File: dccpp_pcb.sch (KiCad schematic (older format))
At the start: 60 parts, among them J1 USB_B_Micro, J10 OSTTC022162, J11 OSTTC022162, J12 OSTTC022162, J2 AVR-ISP-6, J3 OSTTC022162, J4 OSTTC022162, J5 OSTTC022162, J6 OSTTC022162, J7 OSTTC022162, J8 OSTTC022162, J9 OSTTC022162, U1 ATmega32U4-AU, U2 74HC04, U3 IFX007T, U4 IFX007T, U5 IFX007T, U6 IFX007T, Y1 16MHz

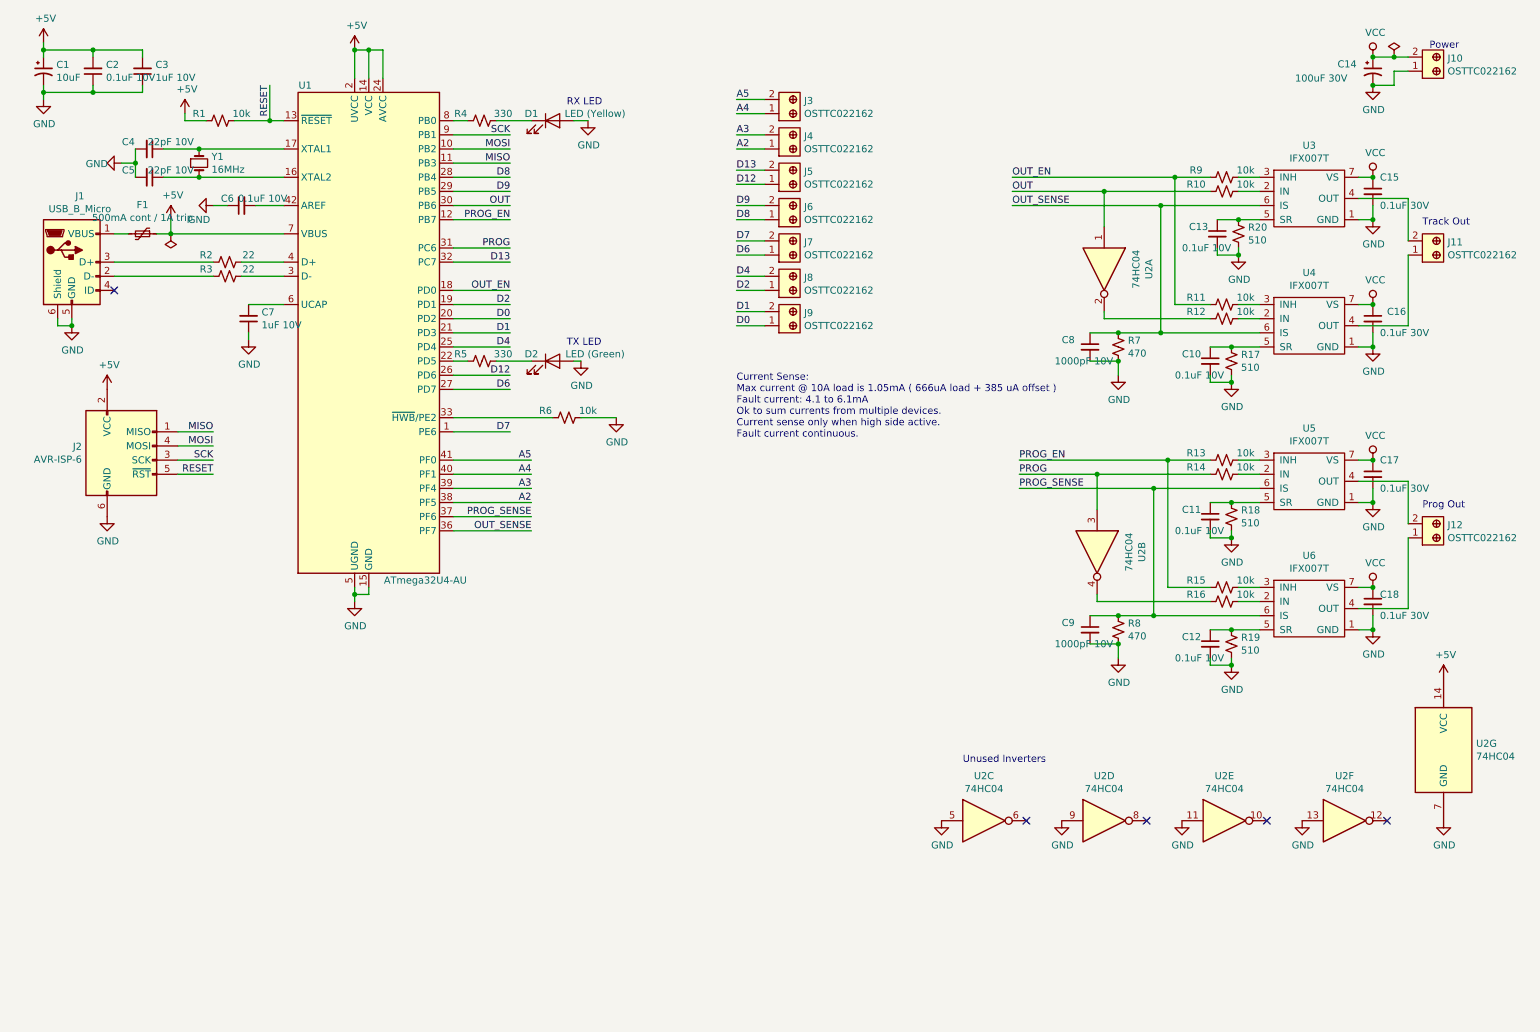
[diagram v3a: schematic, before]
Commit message: Setup design rules
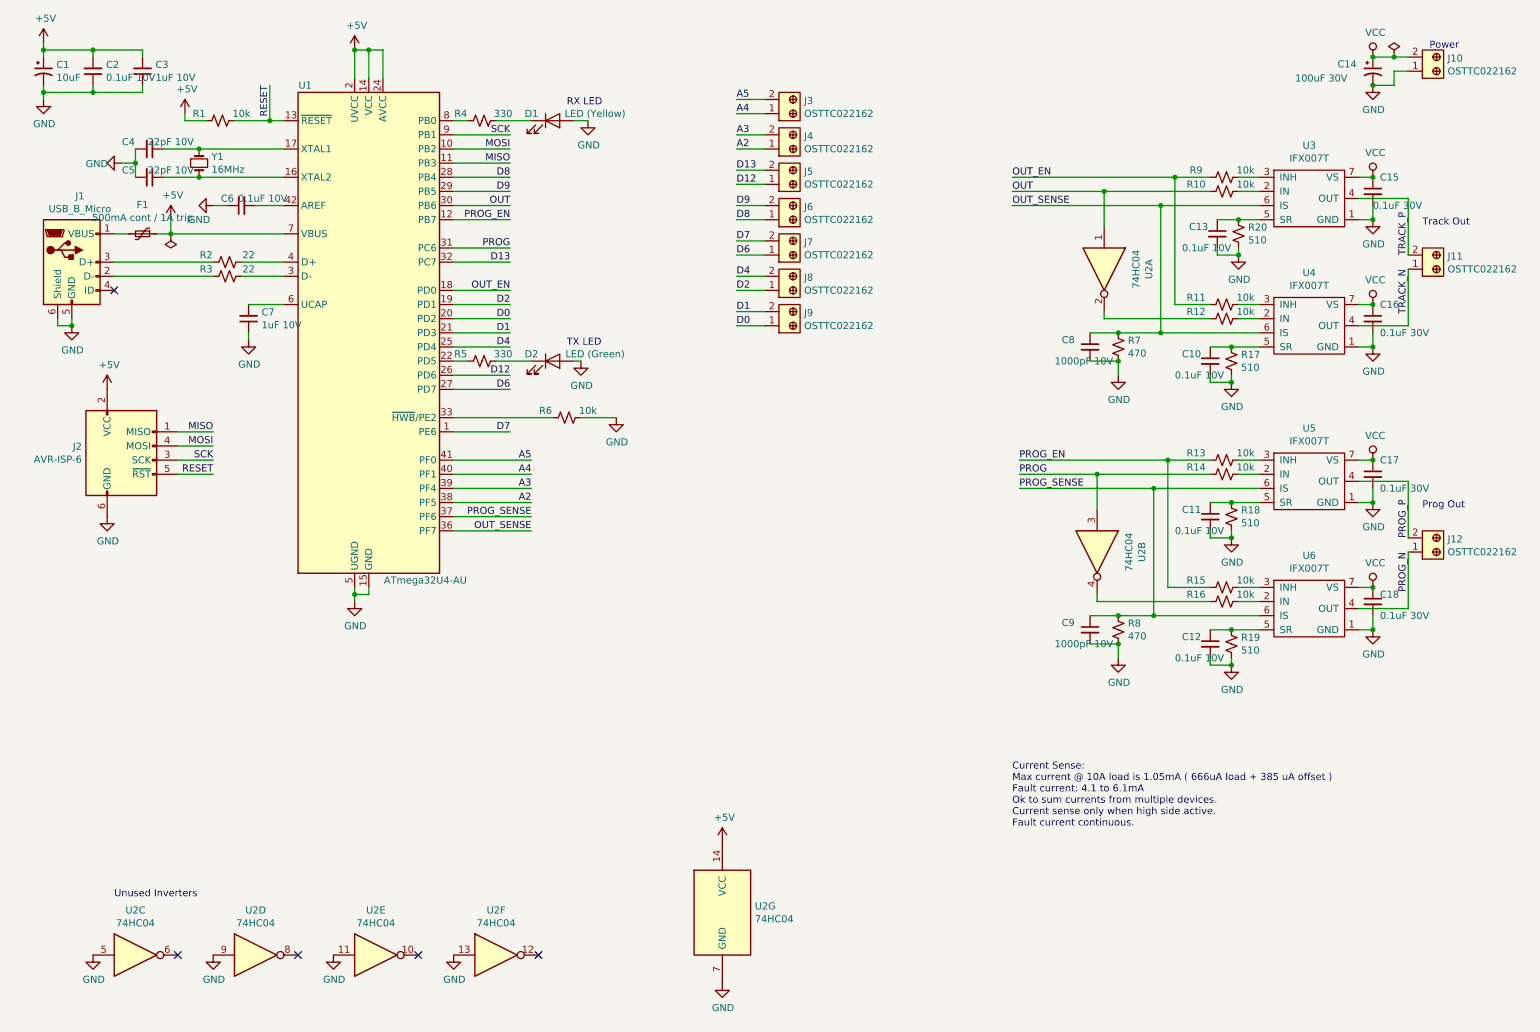
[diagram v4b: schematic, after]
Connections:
- net TRACK_N: now reaches J11.1, U4.4 (OUT), U4.8 (OUT)
- net TRACK_P: now reaches J11.2, U3.4 (OUT), U3.8 (OUT)
- net PROG_P: now reaches J12.2, U5.4 (OUT), U5.8 (OUT)
- net PROG_N: now reaches J12.1, U6.4 (OUT), U6.8 (OUT)
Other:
- moved on the sheet: J11, J12, U2C, U2D, U2E, U2F, U2G

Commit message: Start work on signal layout.
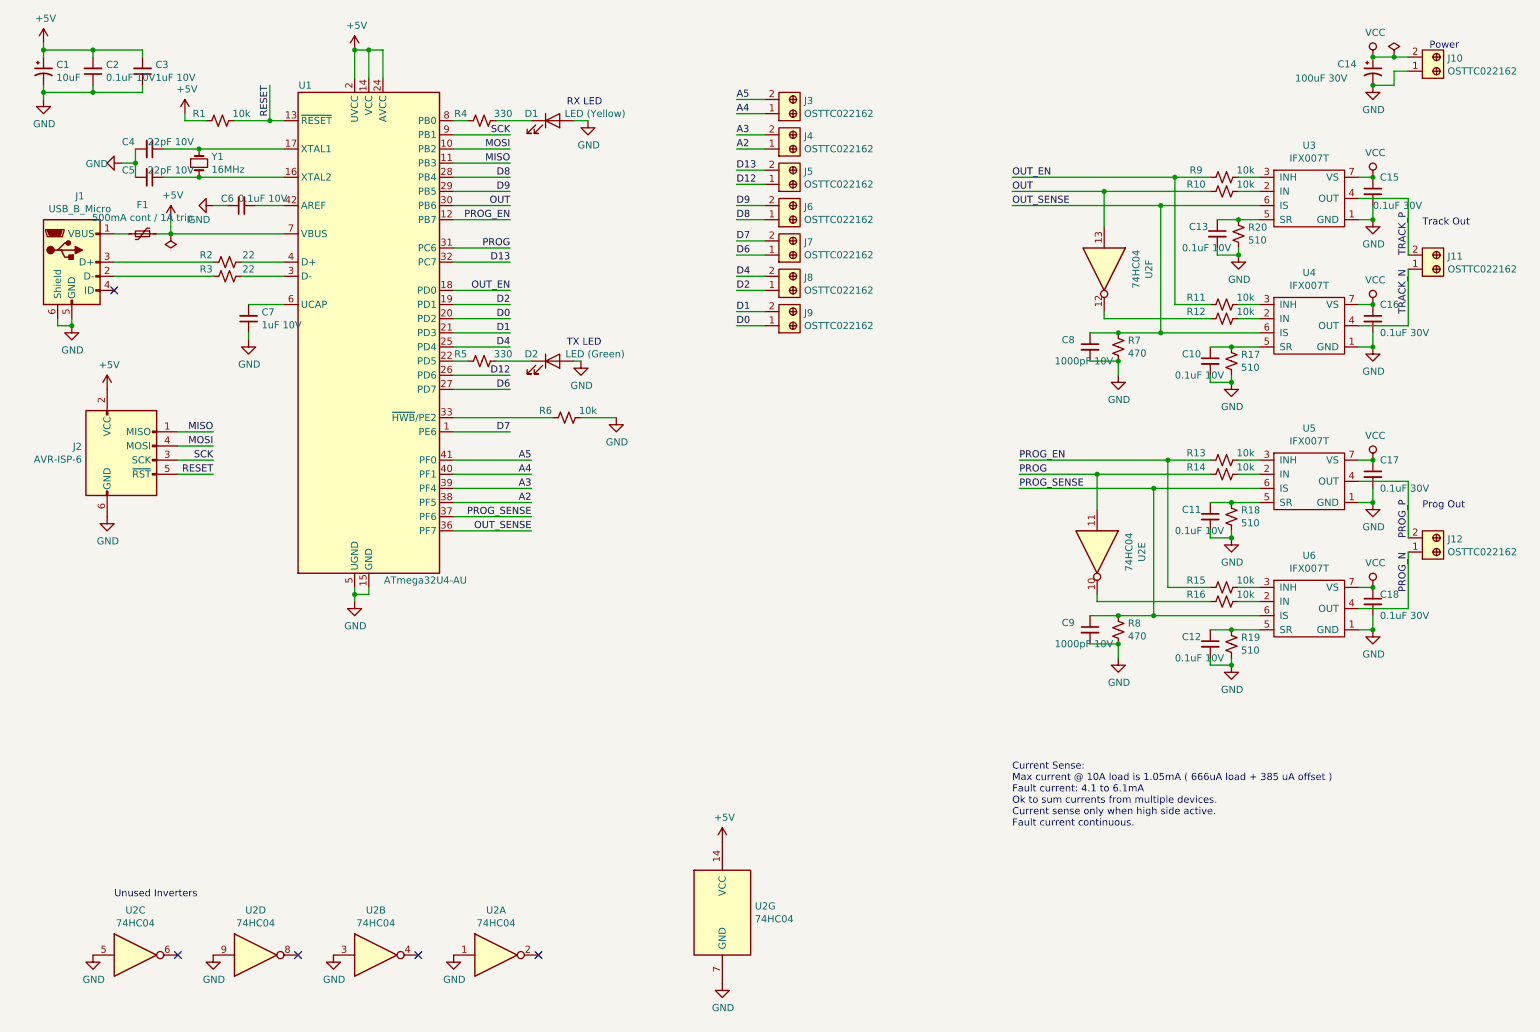
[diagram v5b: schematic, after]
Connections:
- net GND: now also U2.1, U2.3; no longer U2.11, U2.13
- net OUT: now also U2.13; no longer U2.1
- net PROG: now also U2.11; no longer U2.3
- net at U2.2: no longer R12.2
- net at U2.4: no longer R16.2
- net at U2.10: now also R16.2
- net at U2.12: now also R12.2
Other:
- moved on the sheet: U2A, U2B, U2E, U2F
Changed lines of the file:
@@
 EESchema Schematic File Version 4
-LIBS:dccpp_pcb-cache
 EELAYER 29 0
 EELAYER END
@@
 L 74xx:74HC04 U2
 U 1 1 5CF642FD
-P 8200 2350
-F 0 "U2" H 8200 2667 50  0000 C CNN
-F 1 "74HC04" H 8200 2576 50  0000 C CNN
-F 2 "Package_SO:SOIC-14_3.9x8.7mm_P1.27mm" H 8200 2350 50  0001 C CNN
-F 3 "https://assets.nexperia.com/documents/data-sheet/74HC_HCT04.pdf" H 8200 2350 50  0001 C CNN
-F 4 "MC74HC04ADGOS-ND" H 8200 2350 50  0001 C CNN "Digi-Key_PN"
-F 5 "MC74HC04ADG" H 8200 2350 50  0001 C CNN "MPN"
-	1    8200 2350
-	0    1    1    0
+P 3900 7200
+F 0 "U2" H 3900 7517 50  0000 C CNN
+F 1 "74HC04" H 3900 7426 50  0000 C CNN
+F 2 "Package_SO:SOIC-14_3.9x8.7mm_P1.27mm" H 3900 7200 50  0001 C CNN
+F 3 "https://assets.nexperia.com/documents/data-sheet/74HC_HCT04.pdf" H 3900 7200 50  0001 C CNN
+F 4 "MC74HC04ADGOS-ND" H 3900 7200 50  0001 C CNN "Digi-Key_PN"
+F 5 "MC74HC04ADG" H 3900 7200 50  0001 C CNN "MPN"
+	1    3900 7200
+	1    0    0    -1
 $EndComp
 $Comp
 L 74xx:74HC04 U2
 U 2 1 5CF6599A
-P 8150 4350
-F 0 "U2" H 8150 4667 50  0000 C CNN
-F 1 "74HC04" H 8150 4576 50  0000 C CNN
-F 2 "Package_SO:SOIC-14_3.9x8.7mm_P1.27mm" H 8150 4350 50  0001 C CNN
-F 3 "https://assets.nexperia.com/documents/data-sheet/74HC_HCT04.pdf" H 8150 4350 50  0001 C CNN
-F 4 "MC74HC04ADGOS-ND" H 8150 4350 50  0001 C CNN "Digi-Key_PN"
-F 5 "MC74HC04ADG" H 8150 4350 50  0001 C CNN "MPN"
-	2    8150 4350
-	0    1    1    0
+P 3050 7200
+F 0 "U2" H 3050 7517 50  0000 C CNN
+F 1 "74HC04" H 3050 7426 50  0000 C CNN
+F 2 "Package_SO:SOIC-14_3.9x8.7mm_P1.27mm" H 3050 7200 50  0001 C CNN
+F 3 "https://assets.nexperia.com/documents/data-sheet/74HC_HCT04.pdf" H 3050 7200 50  0001 C CNN
+F 4 "MC74HC04ADGOS-ND" H 3050 7200 50  0001 C CNN "Digi-Key_PN"
+F 5 "MC74HC04ADG" H 3050 7200 50  0001 C CNN "MPN"
+	2    3050 7200
+	1    0    0    -1
 $EndComp
 $Comp
@@
 L 74xx:74HC04 U2
 U 5 1 5CF770C1
-P 3050 7200
-F 0 "U2" H 3050 7517 50  0000 C CNN
-F 1 "74HC04" H 3050 7426 50  0000 C CNN
-F 2 "Package_SO:SOIC-14_3.9x8.7mm_P1.27mm" H 3050 7200 50  0001 C CNN
-F 3 "https://assets.nexperia.com/documents/data-sheet/74HC_HCT04.pdf" H 3050 7200 50  0001 C CNN
-F 4 "MC74HC04ADGOS-ND" H 3050 7200 50  0001 C CNN "Digi-Key_PN"
-F 5 "MC74HC04ADG" H 3050 7200 50  0001 C CNN "MPN"
-	5    3050 7200
-	1    0    0    -1
+P 8150 4350
+F 0 "U2" H 8150 4667 50  0000 C CNN
+F 1 "74HC04" H 8150 4576 50  0000 C CNN
+F 2 "Package_SO:SOIC-14_3.9x8.7mm_P1.27mm" H 8150 4350 50  0001 C CNN
+F 3 "https://assets.nexperia.com/documents/data-sheet/74HC_HCT04.pdf" H 8150 4350 50  0001 C CNN
+F 4 "MC74HC04ADGOS-ND" H 8150 4350 50  0001 C CNN "Digi-Key_PN"
+F 5 "MC74HC04ADG" H 8150 4350 50  0001 C CNN "MPN"
+	5    8150 4350
+	0    1    1    0
 $EndComp
 $Comp
 L 74xx:74HC04 U2
 U 6 1 5CF77E52
-P 3900 7200
-F 0 "U2" H 3900 7517 50  0000 C CNN
-F 1 "74HC04" H 3900 7426 50  0000 C CNN
-F 2 "Package_SO:SOIC-14_3.9x8.7mm_P1.27mm" H 3900 7200 50  0001 C CNN
-F 3 "https://assets.nexperia.com/documents/data-sheet/74HC_HCT04.pdf" H 3900 7200 50  0001 C CNN
-F 4 "MC74HC04ADGOS-ND" H 3900 7200 50  0001 C CNN "Digi-Key_PN"
-F 5 "MC74HC04ADG" H 3900 7200 50  0001 C CNN "MPN"
-	6    3900 7200
-	1    0    0    -1
-$EndComp
-$Comp
+P 8200 2350
+F 0 "U2" H 8200 2667 50  0000 C CNN
+F 1 "74HC04" H 8200 2576 50  0000 C CNN
+F 2 "Package_SO:SOIC-14_3.9x8.7mm_P1.27mm" H 8200 2350 50  0001 C CNN
+F 3 "https://assets.nexperia.com/documents/data-sheet/74HC_HCT04.pdf" H 8200 2350 50  0001 C CNN
+F 4 "MC74HC04ADGOS-ND" H 8200 2350 50  0001 C CNN "Digi-Key_PN"
+F 5 "MC74HC04ADG" H 8200 2350 50  0001 C CNN "MPN"
+	6    8200 2350
+	0    1    1    0
+$EndComp
+$Comp

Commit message: More routing
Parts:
- added C19, C20, C21, C22, C23, C24: 0.1uF 10V, Capacitor_SMD:C_0603_1608Metric_Pad1.05x0.95mm_HandSolder, symbol Device:C_Small
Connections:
- net +5V: now also C19.2, C20.2, C21.2, C22.2, C23.2, C24.2
- net GND: now also C19.1, C20.1, C21.1, C22.1, C23.1, C24.1
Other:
- note added: "Place 0.1uF decoupling caps near Vcc on U1 and U2"
- moved on the sheet: C1, C2, C3, C4, C5, C6, C7, D1, D2, F1, J1, J2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

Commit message: Fix crystal
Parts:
- Y1: symbol Device:Crystal_Small -> Device:Crystal_GND24_Small
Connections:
- wire segments 208 -> 210
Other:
- moved on the sheet: C7
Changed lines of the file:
@@
-$EndComp
-$Comp
-L Device:Crystal_Small Y1
-U 1 1 5CD9CF37
-P 1850 2100
-F 0 "Y1" V 1804 2188 50  0000 L CNN
-F 1 "16MHz" V 1895 2188 50  0000 L CNN
-F 2 "Crystal:Crystal_SMD_SeikoEpson_TSX3225-4Pin_3.2x2.5mm_HandSoldering" H 1850 2100 50  0001 C CNN
-F 3 "~" H 1850 2100 50  0001 C CNN
-F 4 "SER4069CT-ND" H 1850 2100 50  0001 C CNN "Digi-Key_PN"
-F 5 "TSX-3225 16.0000MF09Z-AC0" H 1850 2100 50  0001 C CNN "MPN"
-	1    1850 2100
-	0    1    1    0
 $EndComp
 $Comp
@@
 P 1500 2200
 F 0 "C5" V 1450 2050 50  0000 C CNN
-F 1 "22pF 10V" V 1450 2350 50  0000 C CNN
+F 1 "22pF 10V" V 1550 2450 50  0000 C CNN
 F 2 "Capacitor_SMD:C_0603_1608Metric_Pad1.05x0.95mm_HandSolder" H 1500 2200 50  0001 C CNN
 F 3 "~" H 1500 2200 50  0001 C CNN
@@
 P 1500 2000
 F 0 "C4" V 1450 1850 50  0000 C CNN
-F 1 "22pF 10V" V 1450 2150 50  0000 C CNN
+F 1 "22pF 10V" V 1450 2250 50  0000 C CNN
 F 2 "Capacitor_SMD:C_0603_1608Metric_Pad1.05x0.95mm_HandSolder" H 1500 2000 50  0001 C CNN
 F 3 "~" H 1500 2000 50  0001 C CNN
@@
 L Device:C_Small C7
 U 1 1 5CDA0468
-P 2200 3200
-F 0 "C7" H 2108 3154 50  0000 R CNN
-F 1 "1uF 10V" H 2108 3245 50  0000 R CNN
-F 2 "Capacitor_SMD:C_0603_1608Metric_Pad1.05x0.95mm_HandSolder" H 2200 3200 50  0001 C CNN
-F 3 "~" H 2200 3200 50  0001 C CNN
-F 4 "1276-1182-1-ND" H 2200 3200 50  0001 C CNN "Digi-Key_PN"
-F 5 "CL10A105KP8NNNC" H 2200 3200 50  0001 C CNN "MPN"
-	1    2200 3200
+P 2050 3200
+F 0 "C7" H 1958 3154 50  0000 R CNN
+F 1 "1uF 10V" H 1958 3245 50  0000 R CNN
+F 2 "Capacitor_SMD:C_0603_1608Metric_Pad1.05x0.95mm_HandSolder" H 2050 3200 50  0001 C CNN
+F 3 "~" H 2050 3200 50  0001 C CNN
+F 4 "1276-1182-1-ND" H 2050 3200 50  0001 C CNN "Digi-Key_PN"
+F 5 "CL10A105KP8NNNC" H 2050 3200 50  0001 C CNN "MPN"
+	1    2050 3200
 	-1   0    0    1
 $EndComp
@@
 P 2150 2400
 F 0 "C6" V 2200 2500 50  0000 C CNN
-F 1 "0.1uF 10V" V 2200 2250 50  0000 C CNN
+F 1 "0.1uF 10V" V 2250 2250 50  0000 C CNN
 F 2 "Capacitor_SMD:C_0603_1608Metric_Pad1.05x0.95mm_HandSolder" H 2150 2400 50  0001 C CNN
 F 3 "~" H 2150 2400 50  0001 C CNN
@@
 	2250 2400 2450 2400
 Wire Wire Line
-	2200 3100 2450 3100
-Wire Wire Line
-	2450 2200 1850 2200
+	2050 3100 2450 3100
 Wire Wire Line
 	1850 2200 1600 2200
@@
 Wire Wire Line
 	1600 2000 1850 2000
-Wire Wire Line
-	1850 2000 2450 2000
 Connection ~ 1850 2000
 $Comp
@@
 L power:GND #PWR010
 U 1 1 5CDAA31B
-P 2200 3350
-F 0 "#PWR010" H 2200 3100 50  0001 C CNN
-F 1 "GND" H 2205 3177 50  0000 C CNN
-F 2 "" H 2200 3350 50  0001 C CNN
-F 3 "" H 2200 3350 50  0001 C CNN
-	1    2200 3350
-	1    0    0    -1
-$EndComp
-Wire Wire Line
-	2200 3350 2200 3300
+P 2050 3350
+F 0 "#PWR010" H 2050 3100 50  0001 C CNN
+F 1 "GND" H 2055 3177 50  0000 C CNN
+F 2 "" H 2050 3350 50  0001 C CNN
+F 3 "" H 2050 3350 50  0001 C CNN
+	1    2050 3350
+	1    0    0    -1
+$EndComp
+Wire Wire Line
+	2050 3350 2050 3300
 Wire Wire Line
 	1300 2100 1400 2100
@@
 U 1 1 5CDC3346
 P 1450 2600
-F 0 "F1" V 1245 2600 50  0000 C CNN
-F 1 "500mA cont / 1A trip" V 1336 2600 50  0000 C CNN
+F 0 "F1" V 1400 2450 50  0000 C CNN
+F 1 "500mA cont / 1A trip" V 1500 2750 50  0000 C CNN
 F 2 "Fuse:Fuse_1206_3216Metric_Pad1.42x1.75mm_HandSolder" H 1500 2400 50  0001 L CNN
 F 3 "~" H 1450 2600 50  0001 C CNN
@@
 P 1650 2500
 F 0 "#PWR07" H 1650 2350 50  0001 C CNN
-F 1 "+5V" H 1665 2673 50  0000 C CNN
+F 1 "+5V" H 1550 2600 50  0000 C CNN
 F 2 "" H 1650 2500 50  0001 C CNN
 F 3 "" H 1650 2500 50  0001 C CNN
@@
 	4100 1100 3650 1100
 Connection ~ 3650 1100
+Wire Wire Line
+	2450 2200 1850 2200
+Wire Wire Line
+	1850 2000 2450 2000
+$Comp
+L Device:Crystal_GND24_Small Y1
+U 1 1 5CD9CF37
+P 1850 2100
+F 0 "Y1" V 1800 2250 50  0000 L CNN
+F 1 "16MHz" V 1900 2200 50  0000 L CNN
+F 2 "Crystal:Crystal_SMD_SeikoEpson_TSX3225-4Pin_3.2x2.5mm_HandSoldering" H 1850 2100 50  0001 C CNN
+F 3 "~" H 1850 2100 50  0001 C CNN
+F 4 "SER4069CT-ND" H 1850 2100 50  0001 C CNN "Digi-Key_PN"
+F 5 "TSX-3225 16.0000MF09Z-AC0" H 1850 2100 50  0001 C CNN "MPN"
+	1    1850 2100
+	0    1    1    0
+$EndComp
+Wire Wire Line
+	1725 2100 1400 2100
+$Comp
+L power:GND #PWR?
+U 1 1 5D15925A
+P 2200 2100
+F 0 "#PWR?" H 2200 1850 50  0001 C CNN
+F 1 "GND" V 2205 1927 50  0000 C CNN
+F 2 "" H 2200 2100 50  0001 C CNN
+F 3 "" H 2200 2100 50  0001 C CNN
+	1    2200 2100
+	0    -1   -1   0
+$EndComp
+Wire Wire Line
+	1975 2100 2200 2100
 $EndSCHEMATC

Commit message: Add IFX9201 datasheet, symbol and footprint
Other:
- note added: "2.0"
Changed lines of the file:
@@
 EESchema Schematic File Version 4
-LIBS:dccpp_pcb-cache
-EELAYER 29 0
+EELAYER 30 0
 EELAYER END
 $Descr A4 11693 8268
@@
 Wire Wire Line
 	1975 2100 2200 2100
+Text Notes 10650 7650 0    50   ~ 0
+2.0
 $EndSCHEMATC
